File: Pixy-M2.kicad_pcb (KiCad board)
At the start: 4 copper layers, 66 x 100 mm, 78 parts, among them J1 USB_C_Receptacle_USB2.0_14P, J10 SM09B-SRSS-TB, J11 SM06B-SRSS-TB, J4 SM06B-SRSS-TB, J5 SM06B-SRSS-TB, J6 SM06B-SRSS-TB, J7 SM06B-SRSS-TB, J8 S6B-PH-K, J9 S6B-PH-K, Q1 AO4407A, SW1 SW_Push, SW2 SW_Push, SW3 JS102011SAQN, U1 ESP32-S3-WROOM-1-N16, U2 USBLC6-2SC6, U3 AP63203WU, U4 DRV8231ADSG, U5 DRV8231ADSG

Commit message: layout: move J8/J9 to JST SH in the Pololu encoder pin order
J8/J9 were 2.0 mm JST PH wired M1 GND A B VCC M2. The Pololu 12 CPR encoder
on the chosen gearmotors (#5153-#5165) is a 1.0 mm JST SH header wired
GND B A VCC M2 M1, so a 1:1 cable would have put motor voltage on the encoder
supply. Both connectors are now SM06B-SRSS-TB (the J4-J7 part) in Pololu's
order, MP pads to GND, and take Pololu's straight SH-SH cable (#4765-#4769).

SH contacts and that cable are rated 1 A, so R17/R18 go 1.5 -> 2.2 kOhm:
ITRIP 1.47 -> 1.00 A, IPROPI 2.25 -> 3.3 V/A (ADC clips at ~0.94 A).

Schematic: J8/J9 become Conn_01x06_MountingPin (mirrored, so the pin ends stay
on the existing labels); labels re-pinned; MP wired to GND; R17/R18 values and
the two sheet notes updated. Netlist diff shows only those changes; ERC 0.

Board: new last routing stage, tools/autoroute/pololu_conn.py, run by
rework.py after issue8.py. It swaps the footprints for SH clones of J4 (same
rotations, inside the old courtyards), rips the motor trunks back to the
driver escapes, drops other-net copper under the new pad rows (GPIO2/39/40
ran between the old through-hole pins), prunes what that leaves dangling near
the connectors, then re-routes: paired 0.8 mm trunks with 0.6 mm fan-in stubs,
0.2 mm signal reconnections, plane stitches, and U4's VREF feed, whose only 3V3
path under the In2 VBAT island was the old J8 through-hole pin.

                           before        after
  motor A loop area        103.3 mm2     23.9 mm2
  motor B loop area        83.4 mm2      9.8 mm2
  IPROPI to motor copper   0.29 mm       0.53 mm
  vias                     243           253
Other guarded clearances unchanged. Only 13 nets' tracks/vias changed.
DRC: 0 violations, 0 unconnected, 0 parity. Aperture audit passes.

loop.py now finds each pair's connector end by net, so it measures boards
from before and after the re-pin alike.

Co-Authored-By: Claude Opus 5.5 <noreply@anthropic.com>
Claude-Session: https://claude.ai/cod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
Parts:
- J8, J9: value S6B-PH-K -> SM06B-SRSS-TB; footprint Connector_JST:JST_PH_S6B-PH-K_1x06_P2.00mm_Horizontal -> Connector_JST:JST_SH_SM06B-SRSS-TB_1x06-1MP_P1.00mm_Horizontal
- R17, R18: value 1.5kOhm 1% -> 2.2kOhm 1%
- moved J8 5.59 mm to (110.0, 125.5)
- moved J9 4.12 mm to (160.0, 103.4)
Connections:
- J8 pad 1: /MOT_A_1 -> GND
- J8 pad 2: GND -> /GPIO48
- J8 pad 4: /GPIO48 -> /ESP_3V3
- J8 pad 5: /ESP_3V3 -> /MOT_A_2
- J8 pad 6: /MOT_A_2 -> /MOT_A_1
- J9 pad 1: /MOT_B_1 -> GND
- J9 pad 2: GND -> /GPIO38
- J9 pad 4: /GPIO38 -> /ESP_3V3
- J9 pad 5: /ESP_3V3 -> /MOT_B_2
- J9 pad 6: /MOT_B_2 -> /MOT_B_1
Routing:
- net GND: track 95.4 -> 114.9 mm, vias 84 -> 88
- net /ESP_3V3: track 79.9 -> 93.8 mm, vias 26 -> 28
- net /MOT_B_2: track 59.4 -> 51.7 mm, vias 7 -> 8
- net /MOT_A_1: track 16.7 -> 20.3 mm
- net /GPIO38: track 75.3 -> 71.7 mm
- net /MOT_A_2: track 19.0 -> 22.2 mm, vias 1 -> 0
- net /MOT_B_1: track 43.5 -> 46.7 mm, vias 1 -> 0
- net /GPIO39: track 41.6 -> 44.0 mm, vias 2 -> 4
- net /GPIO48: track 26.0 -> 27.5 mm, vias 4 -> 5
- net /GPIO40: track 44.9 -> 46.3 mm, vias 2 -> 4
- net /GPIO47: track 24.6 -> 25.8 mm
- net /GPIO2: track 53.0 -> 53.5 mm

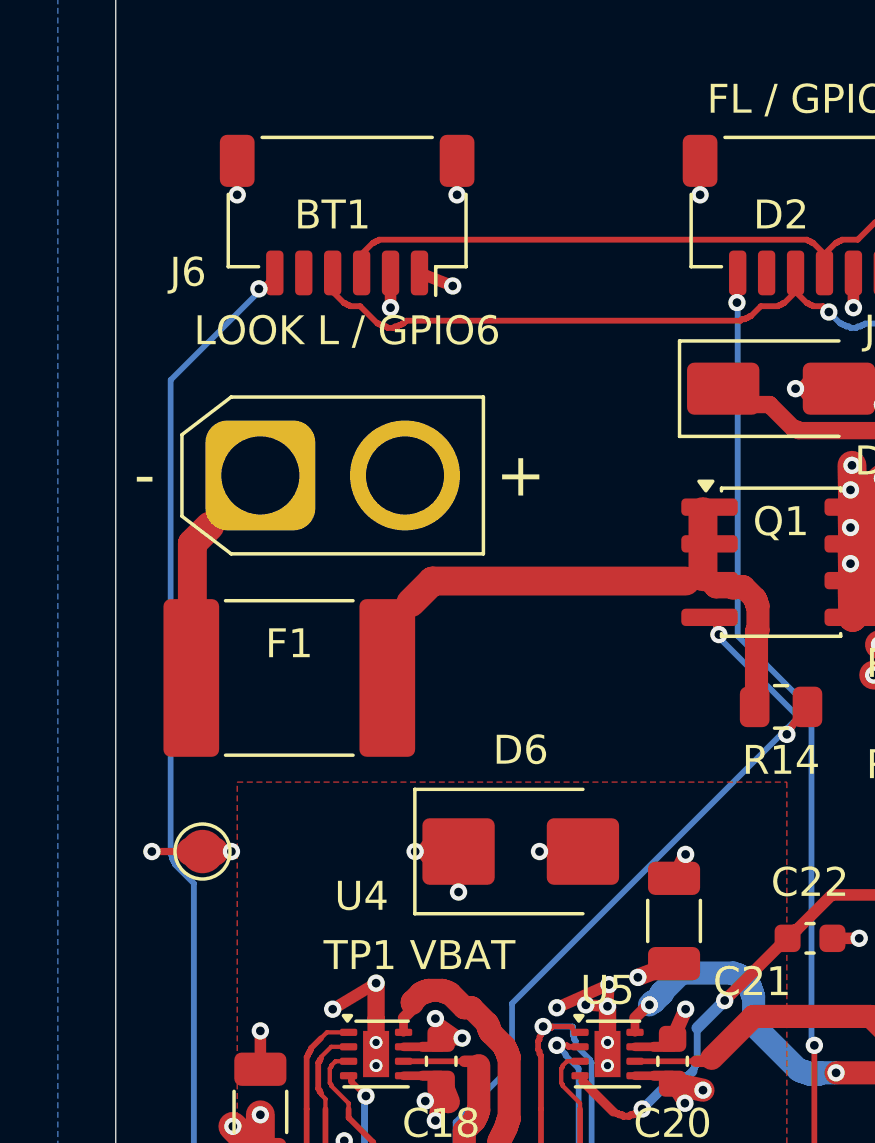
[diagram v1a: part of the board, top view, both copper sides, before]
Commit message: layout: replace F1 with a fuse that breaks the pack's short-circuit current
The chosen pack (OVONIC 2S 450 mAh 100C, XT30) is estimated to put 200-400 A
into a dead short (8-15 mOhm/cell plus connectors, lead, fuse and copper; Ovonic
publishes no internal resistance). The 2920L300/15DR PPTC was rated to break
40 A. A lower-C pack was rejected to keep burst current for the motors, and the
451/453 NANO2 parts (300-400 A @ 32 VDC) sit inside the estimate.

F1 is now a Littelfuse 0885005.DR: 5 A fast-acting, 1500 A @ 125 VDC breaking,
11.9 mOhm. 5 A covers the ~2.4 A worst normal load (both motors at the 1.00 A
limit plus the buck) after the 25% derating. It is one-time: jams are handled
by the drivers' current limit and firmware stall detection. Symbol goes
Device:Polyfuse -> Device:Fuse (same pins); F2 stays a PPTC. Netlist diff:
only F1's value and footprint. ERC 0.

Board: new last routing stage, tools/autoroute/f1_fuse.py. The 16.1 x 7.3 mm
land pattern sits at (110.2, 100.7) between BT1 and Q1; its 7.76 mm courtyard
did not fit the 7.65 mm BT1-D6 gap, so BT1 moves 0.4 mm north (J6 still 2.6 mm
away; verify_placement.py: no underside clashes). /VBAT_RAW and /VBAT_FUSED
re-routed at 1.0 mm; no other net changed. D6's reference moved off F1 pad 2.
DRC: 0 violations, 0 unconnected, 0 parity. Aperture audit passes.

pololu_conn.py fixes found on the way, with J8/J9 copper unchanged:
_zone() uses pad extents rather than centres, and dangling() counts a track
end whose copper overlaps a pad or via as connected.

Co-Authored-By: Claude Opus 5.5 <noreply@anthropic.com>
Claude-Session: https://claude.ai/code/session_01MLrob72MX5PcwtzVMbc3bs
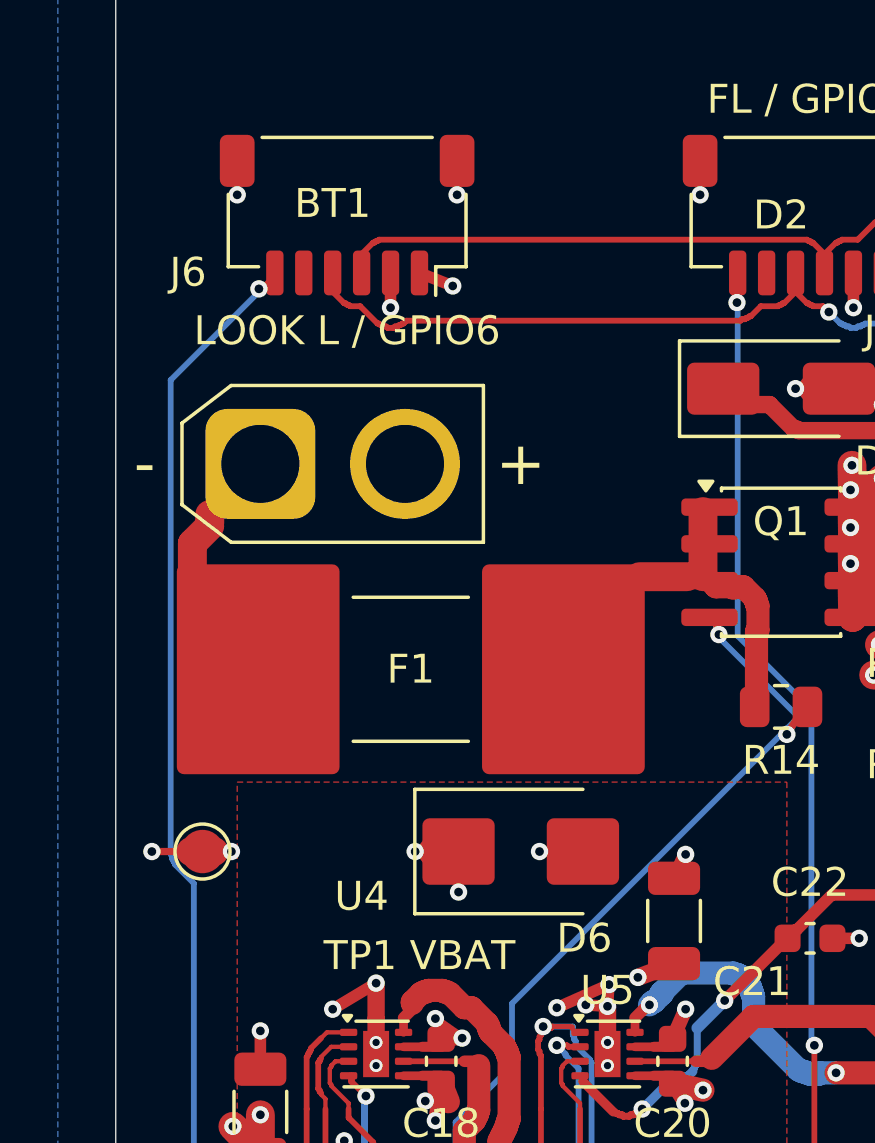
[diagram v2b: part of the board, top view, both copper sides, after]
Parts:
- F1: value 3A 15V -> 5A 1500A@125VDC; footprint Fuse:Fuse_2920_7451Metric -> Fuse:Fuse_Littelfuse-NANO2-885
- moved F1 4.21 mm to (110.2, 100.7)
- moved BT1 0.40 mm to (105.0, 93.6)
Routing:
- net /VBAT_FUSED: track 17.2 -> 9.06 mm

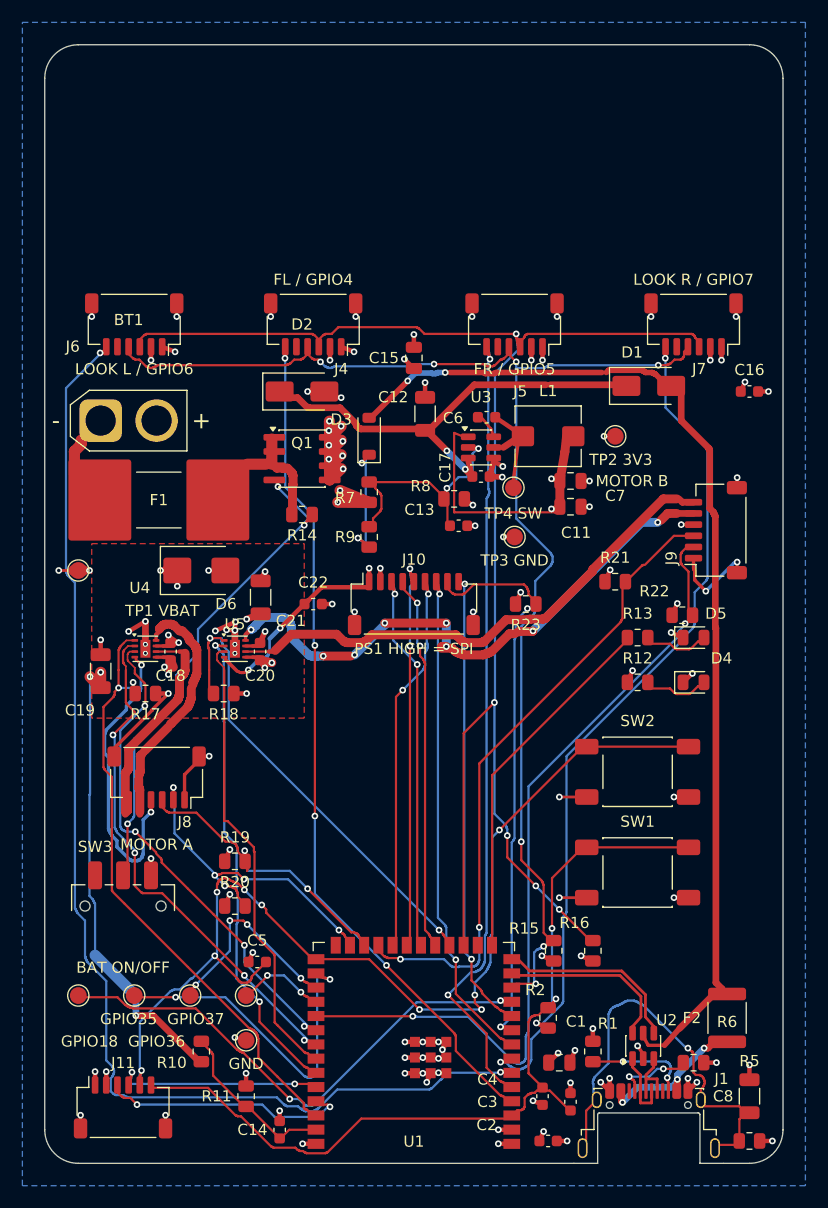
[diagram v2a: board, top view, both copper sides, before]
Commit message: layout: print where the ToF sensors, IMU and motors attach
The mechanical reservations were only on Dwgs.User and User.1/2, which are
not fabricated. assembly_marks.py puts them on the silkscreen:

- F.SilkS: four ToF mount outlines with aim arrows and their connectors
  (J6/J4/J5/J7), and the Adafruit BNO085 outline, holes, chip centre on the
  rotation centre and X/Y axes (+Y forward).
- B.SilkS: both Pololu N20 bodies (gearbox 9 / motor 15 / encoder 8 mm) on
  their wheel axles, motor A left -> J8, motor B right -> J9.

C20 and R15 reference fields move clear of the IMU outline. rework.py runs
the stage after f1_fuse.py. DRC 0 violations, 0 unconnected, 0 parity;
aperture audit passes; tracks and vias unchanged. The B.Cu pour refill
matches a refill of the previous board, whose saved fill was stale.

Co-Authored-By: Claude Opus 5.5 <noreply@anthropic.com>
Claude-Session: https://claude.ai/code/session_01MLrob72MX5PcwtzVMbc3bs
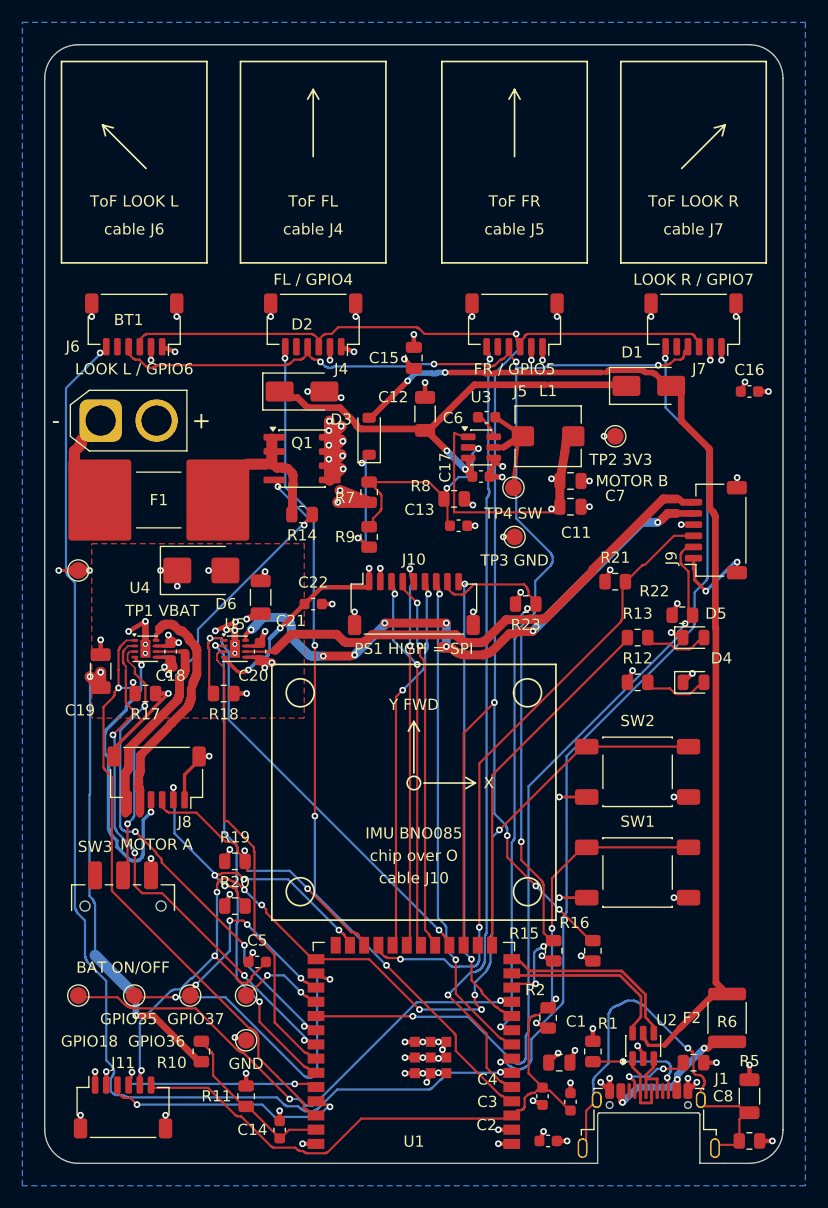
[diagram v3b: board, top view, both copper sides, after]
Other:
- board text added: "ENC"
- board text added: "GEAR"
- board text added: "IMU BNO085"
- board text added: "LEFT J8"
- board text added: "Pololu HP 6V N20"
- board text added: "RIGHT J9"
- board text added: "ToF FL"
- board text added: "ToF FR"
- board text added: "ToF LOOK L"
- board text added: "ToF LOOK R"
- board text added: "WHEEL"
- board text added: "X"
- board text added: "Y FWD"
- board text added: "cable J10"
- board text added: "cable J4"
- board text added: "cable J5"
- board text added: "cable J6"
- board text added: "cable J7"
- board text added: "chip over O"

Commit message: layout: reserve the battery bay between the axles
The placement-era battery reservation (40 x 30 x 15 mm at board x 13-53,
y 5-35) predates the pack. The OVONIC 2S 450 mAh (62 x 17 x 14 mm) fits
it neither way round. The front strip does fit, but with the wheels at
y 50 and 82 it moves the estimated CG about 6 mm ahead of the front axle.

The pack now lies across the underside between the two motors, at
x 0.5-62.5, y 57.5-74.5, with its centre on the rotation centre's y.
Its rule area runs to the right edge to cover the lead exit.

The motors' 4 mm encoder allowance, which used to face the middle of the
board, now faces outboard. Pololu's encoder board stands 3-4 mm proud of
one face of the gearmotor, so each motor is mounted with that face
outboard. The inboard attachment bands and the battery strap bands are
deleted, and the outboard bands move out with their envelopes. User.2
shows the lead route to BT1, about 13 cm long.

tools/autoroute/battery_bay.py does the edit as a rework.py stage and
checks every drilled pad against the new envelopes: no clashes. A full
rework.py regeneration reproduces the edited board item for item. DRC is
0 violations, 0 unconnected and 0 parity issues, and the aperture audit
passes. Copper is unchanged.

Co-Authored-By: Claude Opus 5.5 <noreply@anthropic.com>
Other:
- board text added: "BATTERY (bottom) 62 x 17 x 14"
- board text added: "BATTERY LEAD: XT30 around the left edge to BT1"
- board text removed: "BATTERY (bottom) 40 x 30 x 15"
